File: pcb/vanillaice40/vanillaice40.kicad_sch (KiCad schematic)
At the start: 106 parts, among them J1 FX18-120S-0.8SV20, J2 SM04B-SRSS-TBLFSN, J3 Conn_01x02_Pin, SW3 RESET, U1 TPS563252DRLR, U2 ICE40HX4K-TQ144, U3 W25X40CLSN, U4 TPS563252DRLR, U5 FT2232HL, U6 93LCxxBxxOT, X1 SG-8101CE 100Mhz, Y1 12Mhz/18pf

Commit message: all tracks down
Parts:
- removed C3: 0.1uf, Capacitor_SMD:C_0402_1005Metric, symbol Device:C_Small
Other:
- moved on the sheet: C2, C44
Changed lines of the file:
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@@
 	)
 	(junction
-		(at 298.45 27.94)
-		(diameter 0)
-		(color 0 0 0 0)
-	)
-	(junction
 		(at 90.17 128.27)
 		(diameter 0)
@@
 	)
 	(junction
-		(at 288.29 38.1)
+		(at 298.45 38.1)
 		(diameter 0)
 		(color 0 0 0 0)
@@
 	)
 	(junction
-		(at 298.45 38.1)
-		(diameter 0)
-		(color 0 0 0 0)
-	)
-	(junction
 		(at 129.54 129.54)
 		(diameter 0)
@@
 	)
 	(junction
-		(at 288.29 27.94)
+		(at 298.45 27.94)
 		(diameter 0)
 		(color 0 0 0 0)
@@
 	(wire
 		(pts
-			(xy 278.13 30.48) (xy 278.13 27.94)
+			(xy 288.29 30.48) (xy 288.29 27.94)
 		)
 		(stroke
@@
 	(wire
 		(pts
-			(xy 278.13 38.1) (xy 288.29 38.1)
+			(xy 288.29 38.1) (xy 298.45 38.1)
 		)
 		(stroke
@@
 	(wire
 		(pts
-			(xy 298.45 35.56) (xy 298.45 38.1)
-		)
-		(stroke
-			(width 0)
-			(type default)
-		)
-	)
-	(wire
-		(pts
 			(xy 384.81 180.34) (xy 394.97 180.34)
 		)
@@
 	(wire
 		(pts
-			(xy 298.45 38.1) (xy 309.88 38.1)
-		)
-		(stroke
-			(width 0)
-			(type default)
-		)
-	)
-	(wire
-		(pts
 			(xy 407.67 137.16) (xy 407.67 139.7)
 		)
@@
 	(wire
 		(pts
-			(xy 288.29 35.56) (xy 288.29 38.1)
+			(xy 298.45 35.56) (xy 298.45 38.1)
 		)
 		(stroke
@@
 	(wire
 		(pts
-			(xy 288.29 38.1) (xy 298.45 38.1)
+			(xy 298.45 38.1) (xy 309.88 38.1)
 		)
 		(stroke
@@
 	(wire
 		(pts
-			(xy 288.29 27.94) (xy 288.29 30.48)
+			(xy 298.45 27.94) (xy 298.45 30.48)
 		)
 		(stroke
@@
 	(wire
 		(pts
-			(xy 278.13 35.56) (xy 278.13 38.1)
+			(xy 288.29 35.56) (xy 288.29 38.1)
 		)
 		(stroke
@@
 	(wire
 		(pts
-			(xy 278.13 27.94) (xy 288.29 27.94)
+			(xy 288.29 27.94) (xy 298.45 27.94)
 		)
 		(stroke
@@
 	(wire
 		(pts
-			(xy 298.45 27.94) (xy 298.45 30.48)
-		)
-		(stroke
-			(width 0)
-			(type default)
-		)
-	)
-	(wire
-		(pts
 			(xy 254 152.4) (xy 264.16 152.4)
 		)
@@
 	(wire
 		(pts
-			(xy 288.29 27.94) (xy 298.45 27.94)
-		)
-		(stroke
-			(width 0)
-			(type default)
-		)
-	)
-	(wire
-		(pts
 			(xy 81.28 177.8) (xy 81.28 185.42)
 		)
@@
 		)
 	)
-	(label "IOL_3B"
-		(at 295.91 318.77 0)
-		(fields_autoplaced yes)
-		(effects
-			(font
-				(size 1.27 1.27)
-			)
-			(justify left bottom)
-		)
-	)
 	(label "IOR_128"
 		(at 320.04 180.34 0)
@@
 		)
 	)
-	(label "IOL_3A"
-		(at 295.91 316.23 0)
-		(fields_autoplaced yes)
-		(effects
-			(font
-				(size 1.27 1.27)
-			)
-			(justify left bottom)
-		)
-	)
 	(label "IOB_96"
 		(at 351.79 215.9 0)
@@
 		)
 	)
-	(label "IOL_2A"
-		(at 295.91 311.15 0)
-		(fields_autoplaced yes)
-		(effects
-			(font
-				(size 1.27 1.27)
-			)
-			(justify left bottom)
-		)
-	)
 	(label "USB_DP"
 		(at 55.88 57.15 0)
@@
 		)
 	)
-	(label "IOL_2B"
-		(at 295.91 313.69 0)
-		(fields_autoplaced yes)
-		(effects
-			(font
-				(size 1.27 1.27)
-			)
-			(justify left bottom)
-		)
-	)
 	(label "IOL_18A"
 		(at 227.33 167.64 0)
@@
 	(symbol
 		(lib_id "Device:C_Small")
-		(at 288.29 33.02 0)
+		(at 298.45 33.02 0)
 		(unit 1)
 		(exclude_from_sim no)
@@
 		(fields_autoplaced yes)
 		(property "Reference" "C44"
-			(at 290.83 31.7562 0)
+			(at 300.99 31.7562 0)
 			(effects
 				(font
@@
 		)
 		(property "Value" "0.1uf"
-			(at 290.83 34.2962 0)
+			(at 300.99 34.2962 0)
 			(effects
 				(font
@@
 		)
 		(property "Footprint" "Capacitor_SMD:C_0402_1005Metric"
-			(at 288.29 33.02 0)
+			(at 298.45 33.02 0)
 			(effects
 				(font
@@
 		)
 		(property "Datasheet" "~"
-			(at 288.29 33.02 0)
+			(at 298.45 33.02 0)
 			(effects
 				(font
@@
 		)
 		(property "Description" "Unpolarized capacitor, small symbol"
-			(at 288.29 33.02 0)
+			(at 298.45 33.02 0)
 			(effects
 				(font
@@
 		)
 		(property "MFG_Part" ""
-			(at 288.29 33.02 0)
+			(at 298.45 33.02 0)
 			(effects
 				(font
@@
 	)
 	(symbol
-		(lib_id "Device:C_Small")
-		(at 298.45 33.02 0)
-		(unit 1)
-		(exclude_from_sim no)
-		(in_bom yes)
-		(on_board yes)
-		(dnp no)
-		(fields_autoplaced yes)
-		(property "Reference" "C3"
-			(at 300.99 31.7562 0)
-			(effects
-				(font
-					(size 1.27 1.27)
-				)
-				(justify left)
-			)
-		)
-		(property "Value" "0.1uf"
-			(at 300.99 34.2962 0)
-			(effects
-				(font
-					(size 1.27 1.27)
-				)
-				(justify left)
-			)
-		)
-		(property "Footprint" "Capacitor_SMD:C_0402_1005Metric"
-			(at 298.45 33.02 0)
-			(effects
-				(font
-					(size 1.27 1.27)
-				)
-				(hide yes)
-			)
-		)
-		(property "Datasheet" "~"
-			(at 298.45 33.02 0)
-			(effects
-				(font
-					(size 1.27 1.27)
-				)
-				(hide yes)
-			)
-		)
-		(property "Description" "Unpolarized capacitor, small symbol"
-			(at 298.45 33.02 0)
-			(effects
-				(font
-					(size 1.27 1.27)
-				)
-				(hide yes)
-			)
-		)
-		(property "MFG_Part" ""
-			(at 298.45 33.02 0)
-			(effects
-				(font
-					(size 1.27 1.27)
-				)
-				(hide yes)
-			)
-		)
-		(pin "2"
-		)
-		(pin "1"
-		)
-		(instances
-			(project "vanillaice40"
-				(path "/a9f93d6d-ad6a-4eb5-8259-93de27758801"
-					(reference "C3")
-					(unit 1)
-				)
-			)
-		)
-	)
-	(symbol
 		(lib_id "power:+3V3")
 		(at 321.31 52.07 0)
@@
 	(symbol
 		(lib_id "Device:C_Small")
-		(at 278.13 33.02 0)
+		(at 288.29 33.02 0)
 		(unit 1)
 		(exclude_from_sim no)
@@
 		(fields_autoplaced yes)
 		(property "Reference" "C2"
-			(at 280.67 31.7562 0)
+			(at 290.83 31.7562 0)
 			(effects
 				(font
@@
 		)
 		(property "Value" "22uf"
-			(at 280.67 34.2962 0)
+			(at 290.83 34.2962 0)
 			(effects
 				(font
@@
 		)
 		(property "Footprint" "Capacitor_SMD:C_0603_1608Metric"
-			(at 278.13 33.02 0)
+			(at 288.29 33.02 0)
 			(effects
 				(font
@@
 		)
 		(property "Datasheet" "~"
-			(at 278.13 33.02 0)
+			(at 288.29 33.02 0)
 			(effects
 				(font
@@
 		)
 		(property "Description" "Unpolarized capacitor, small symbol"
-			(at 278.13 33.02 0)
+			(at 288.29 33.02 0)
 			(effects
 				(font
@@
 		)
 		(property "MFG_Part" ""
-			(at 278.13 33.02 0)
+			(at 288.29 33.02 0)
 			(effects
 				(font

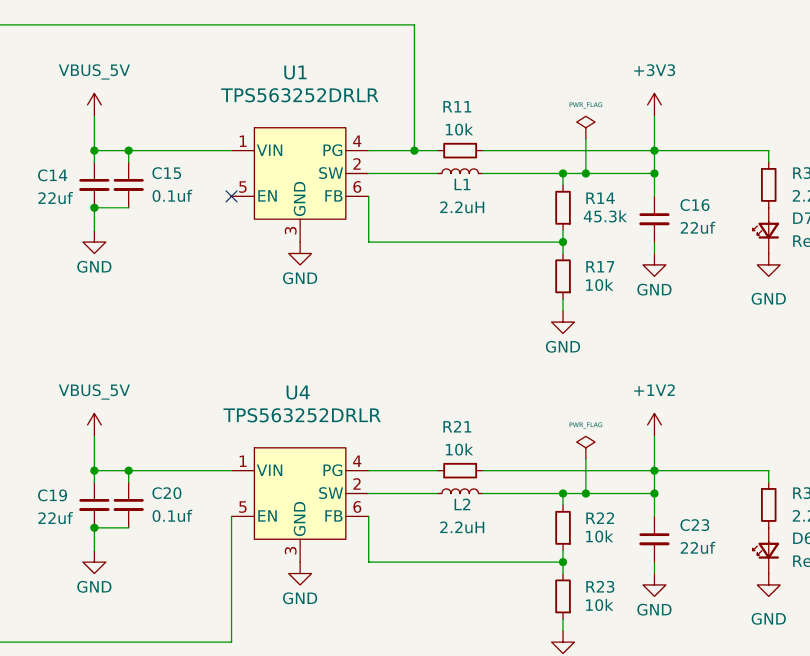
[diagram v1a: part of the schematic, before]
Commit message: zones for regulators
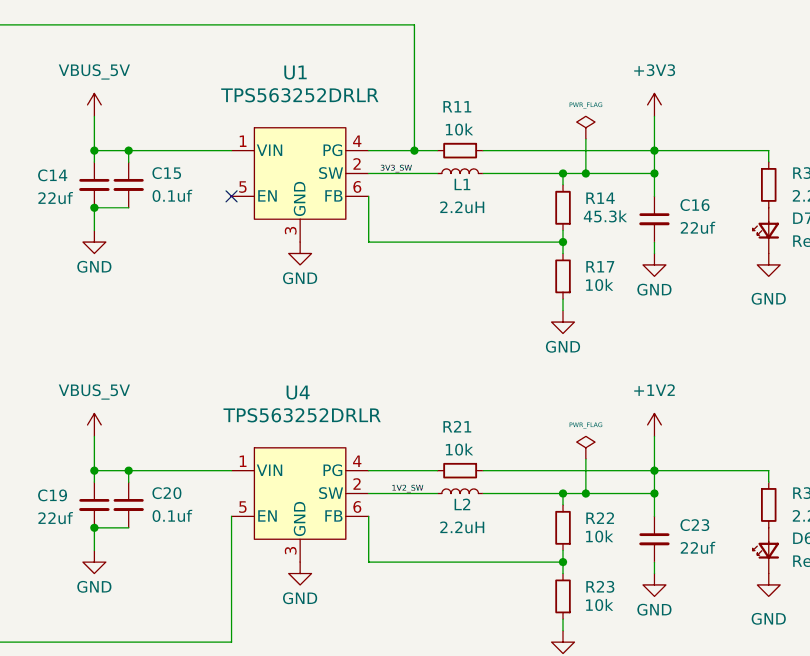
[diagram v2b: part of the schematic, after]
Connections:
- net 1V2_SW: now reaches L2.1, U4.2 (SW)
- net 3V3_SW: now reaches L1.1, U1.2 (SW)
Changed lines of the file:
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@@
+		)
+	)
+	(label "3V3_SW"
+		(at 233.68 73.66 0)
+		(fields_autoplaced yes)
+		(effects
+			(font
+				(size 0.635 0.635)
+			)
+			(justify left bottom)
 		)
 	)
@@
 			)
 			(justify left bottom)
+		)
+	)
+	(label "1V2_SW"
+		(at 234.95 109.22 0)
+		(fields_autoplaced yes)
+		(effects
+			(font
+				(size 0.635 0.635)
+			)
+			(justify left bottom)

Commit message: ergonomic labels
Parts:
- RESET1: renamed from SW3; value RESET -> SPDT
- renumbered D6 to 1V2_1, D7 to 3V3_1, D4 to 5V_1, C14 to C13, C15 to C14, C13 to C15, C44 to C3, D5 to CDONE1, D3 to D1, J3 to J1, J1 to J3, R12 to R10, R39 to R11, R14 to R12, R15 to R13, R13 to R14, R16 to R15, R17 to R16, R18 to R17, R19 to R18, R20 to R19, R21 to R20, R38 to R21, R6 to R3, R3 to R4, R4 to R5, R5 to R6, R9 to R7, R10 to R8, R11 to R9, D1 to USR1, D2 to USR2

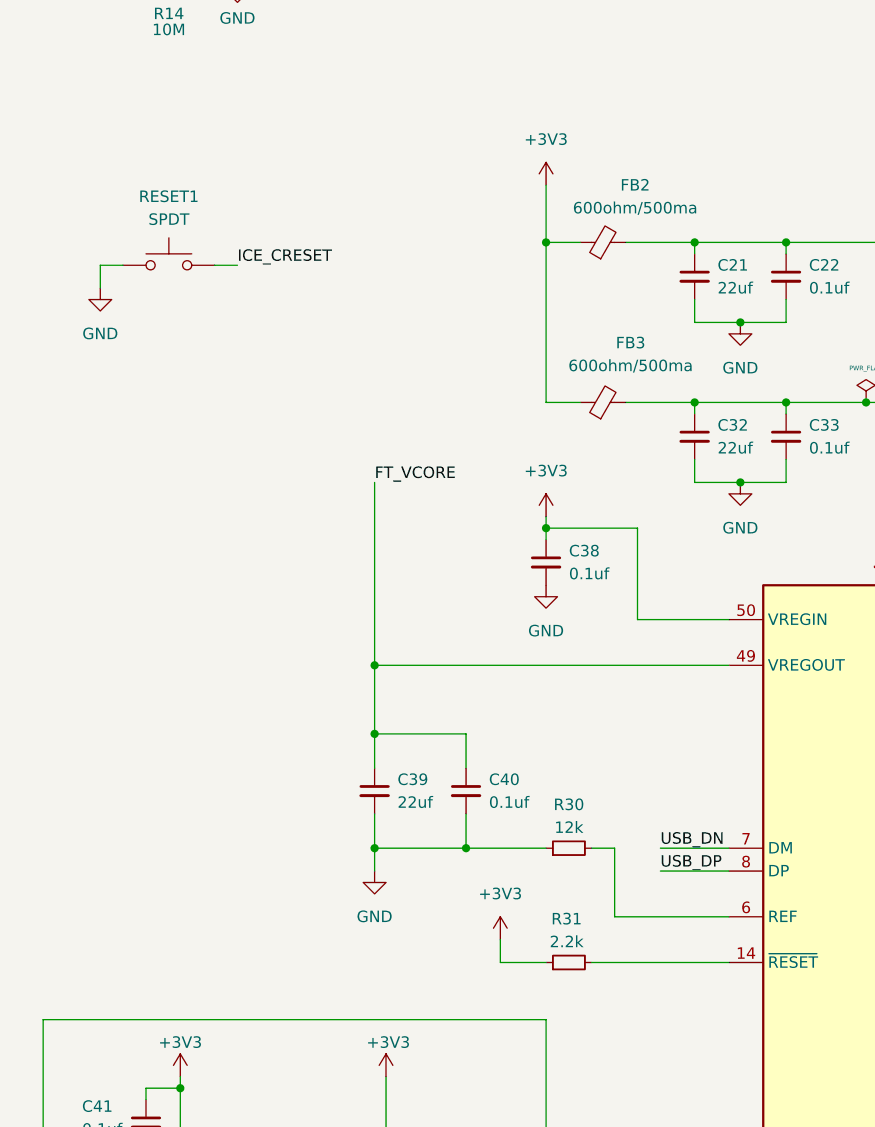
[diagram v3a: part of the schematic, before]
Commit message: add flash spi header
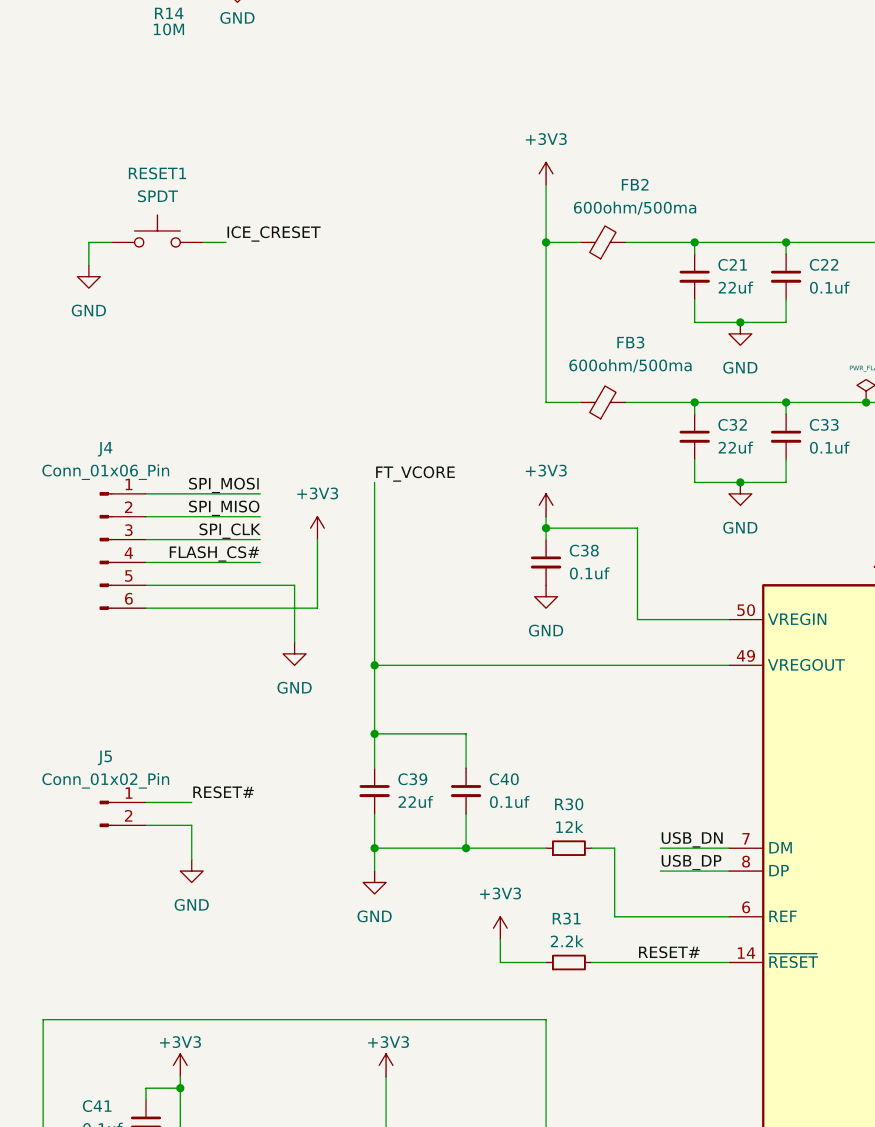
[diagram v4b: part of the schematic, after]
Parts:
- added J4: Conn_01x06_Pin, Connector_PinHeader_2.54mm:PinHeader_1x06_P2.54mm_Vertical, symbol Connector:Conn_01x06_Pin
- added J5: Conn_01x02_Pin, Connector_PinHeader_2.54mm:PinHeader_1x02_P2.54mm_Vertical, symbol Connector:Conn_01x02_Pin
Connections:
- net +3V3: now also J4.6 (Pin_6)
- net FLASH_CS#: now also J4.4 (Pin_4)
- net GND: now also J4.5 (Pin_5), J5.2 (Pin_2)
- net SPI_CLK: now also J4.3 (Pin_3)
- net SPI_MISO: now also J4.2 (Pin_2)
- net SPI_MOSI: now also J4.1 (Pin_1)
- net RESET#: now reaches R31.2, U5.14 (~{RESET})
- net RESET#: now also J5.1 (Pin_1)
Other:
- moved on the sheet: RESET1

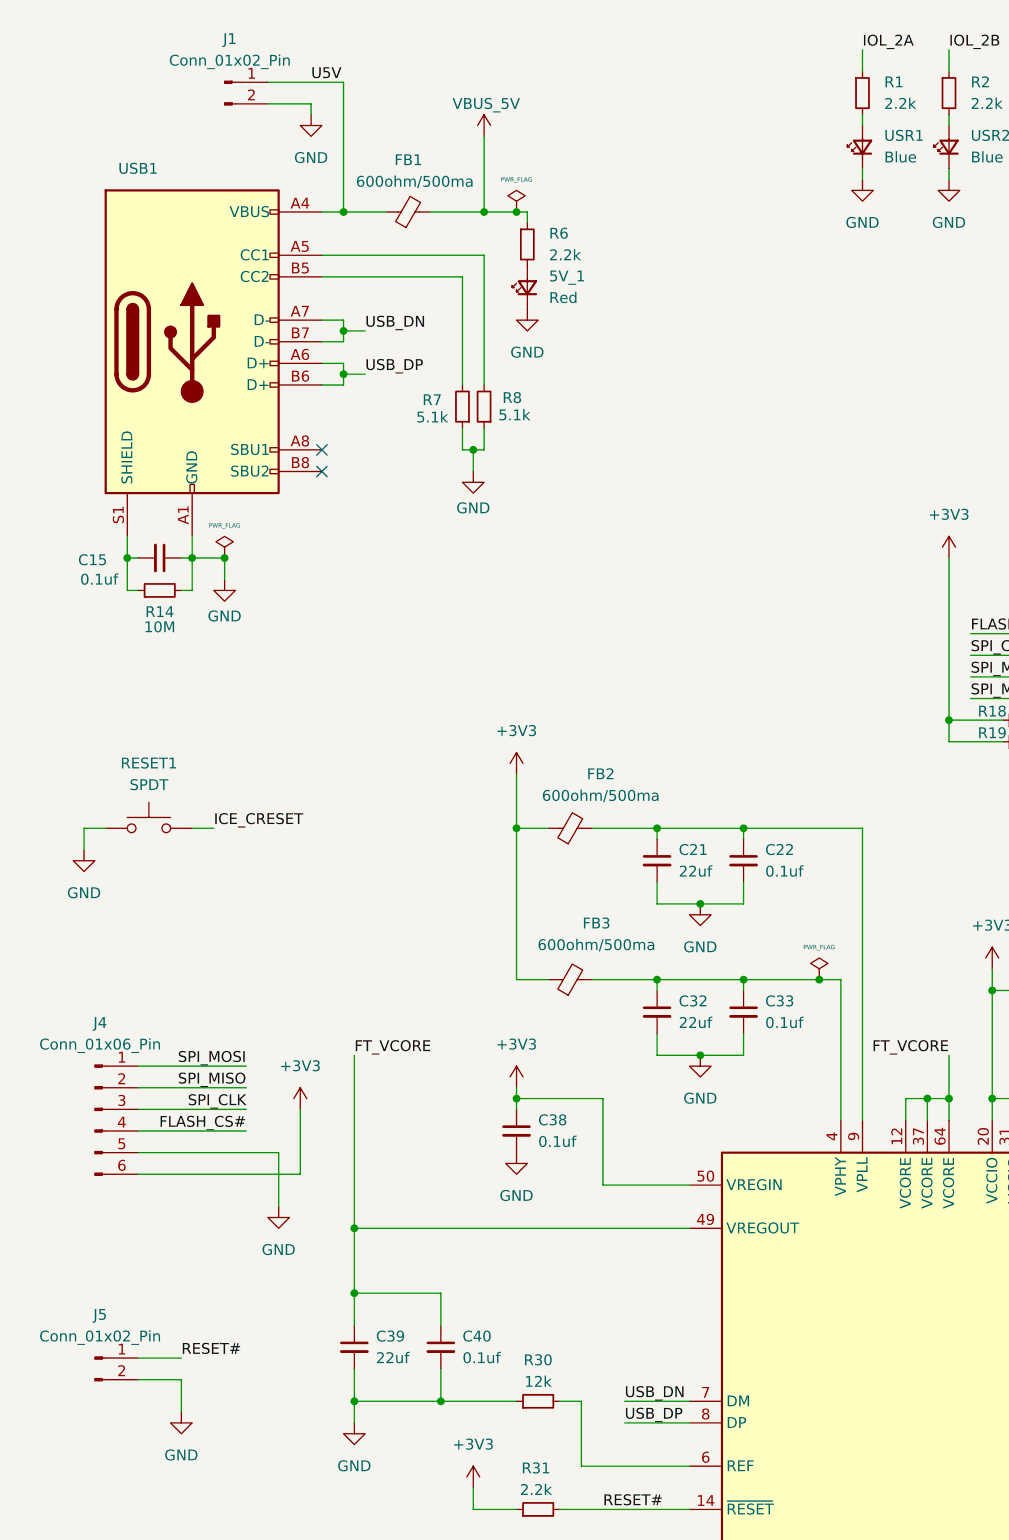
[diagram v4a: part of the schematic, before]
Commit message: add logo
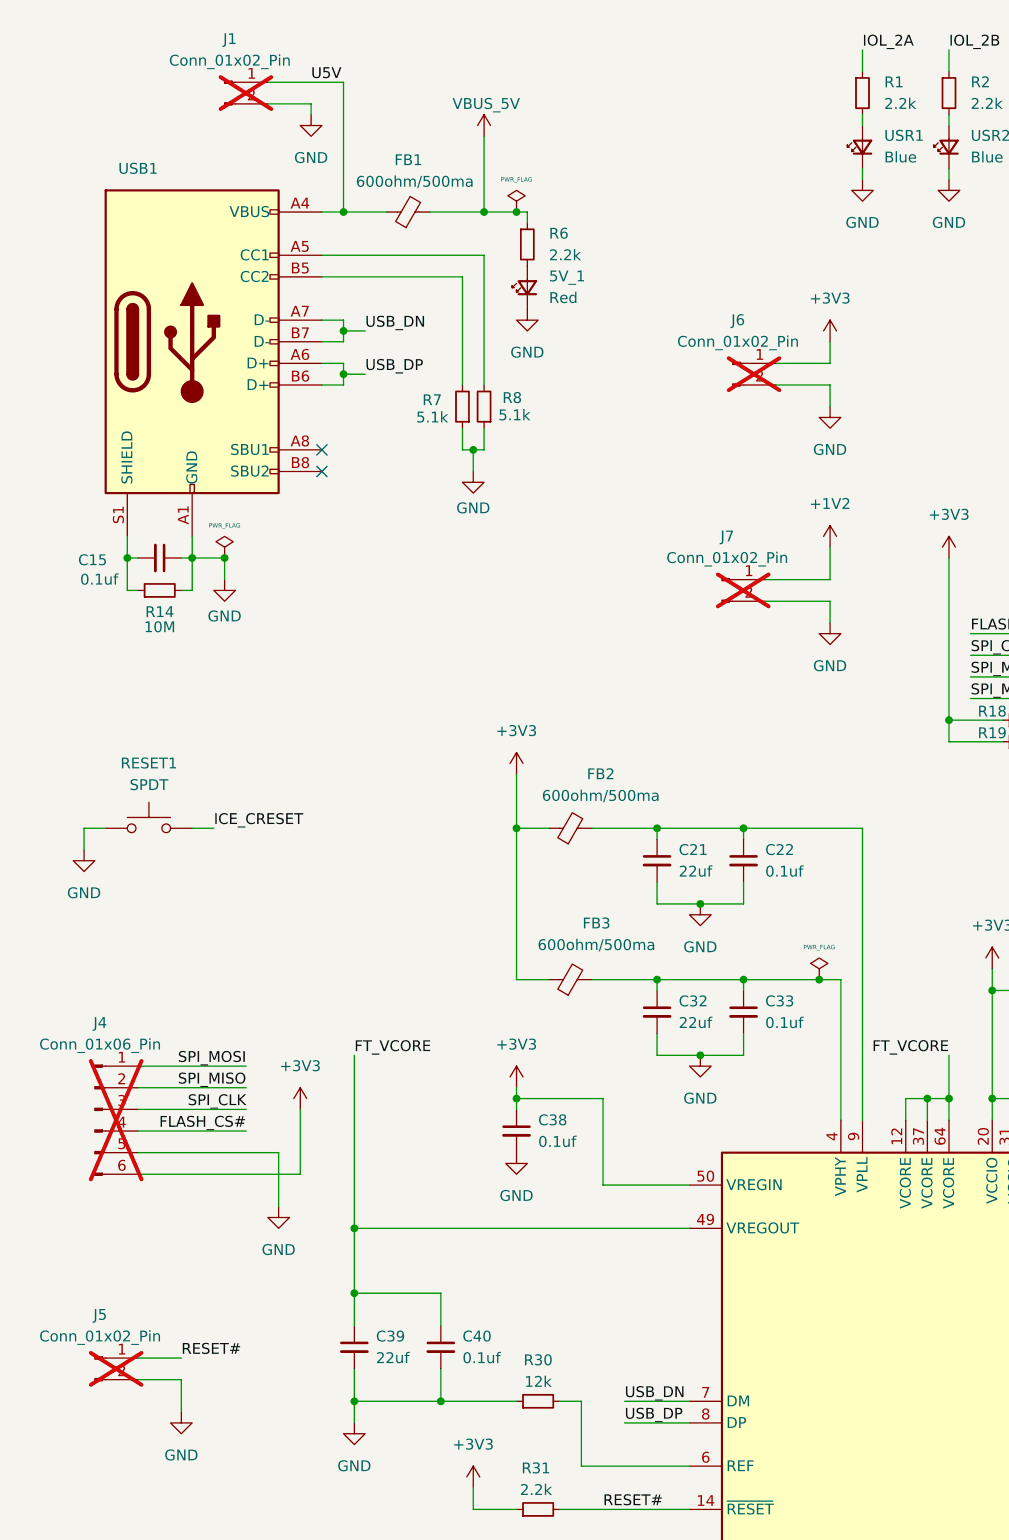
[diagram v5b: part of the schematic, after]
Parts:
- added J6, J7: Conn_01x02_Pin, Connector_PinHeader_2.54mm:PinHeader_1x02_P2.54mm_Vertical, symbol Connector:Conn_01x02_Pin
- J1, J4, J5: now not fitted; now left out of the parts list
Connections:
- net +1V2: now also J7.1 (Pin_1)
- net +3V3: now also J6.1 (Pin_1)
- net GND: now also J6.2 (Pin_2), J7.2 (Pin_2)

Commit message: add fab toolkit and setup
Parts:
- L1, L2: MFG_Part DFE252012P-2R2M=P2 -> (none)
- USB1: MPN GT-USB-7004 -> (none)
